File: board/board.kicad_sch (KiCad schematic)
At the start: 3 parts, among them J1 022_battery_cells, J2 022_battery_cells

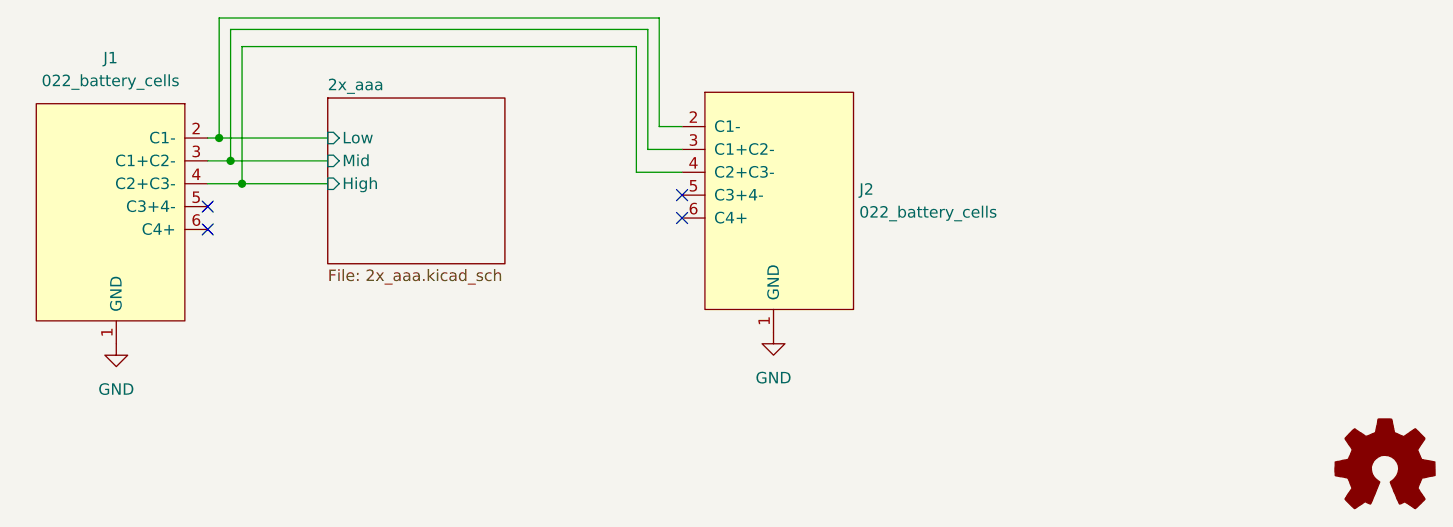
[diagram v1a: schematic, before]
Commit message: changed to 18650 holder
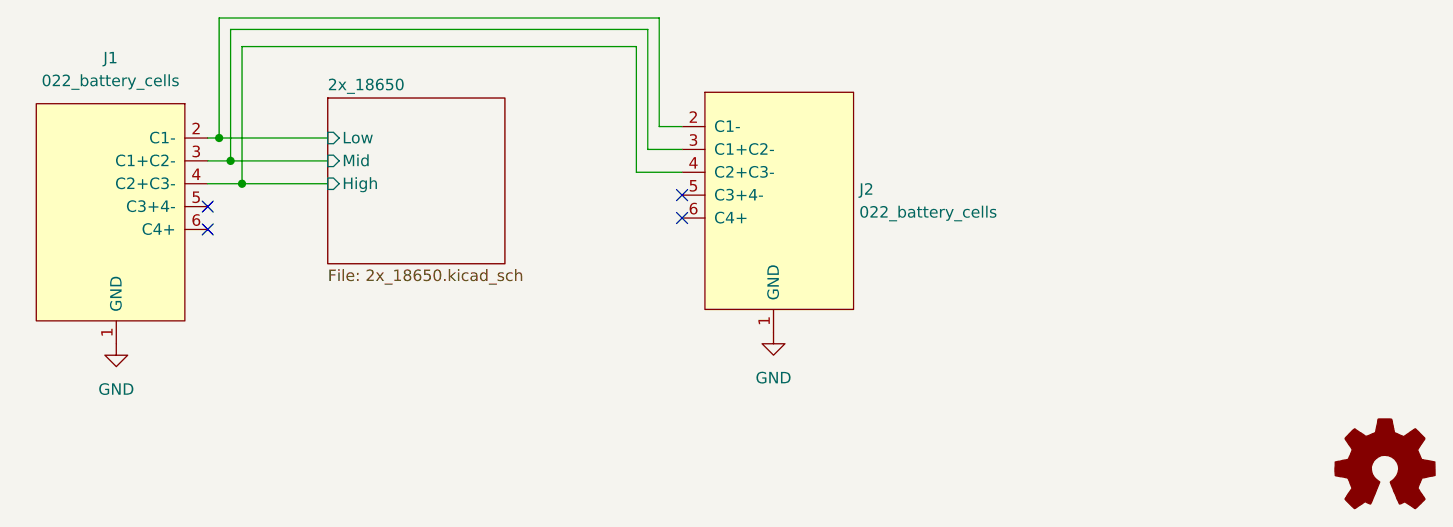
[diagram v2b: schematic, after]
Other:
- sheet 2x_aaa renamed 2x_18650
- sheet 2x_18650: file 2x_aaa.kicad_sch -> 2x_18650.kicad_sch
